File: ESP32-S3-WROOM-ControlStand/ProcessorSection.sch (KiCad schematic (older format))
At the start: 21 parts, among them IC601 USBLC6-2SC6, J601 GCT_USB4105, SW24 RESET, SW601 BOOT, U601 ESP32_S3_WROOM-1

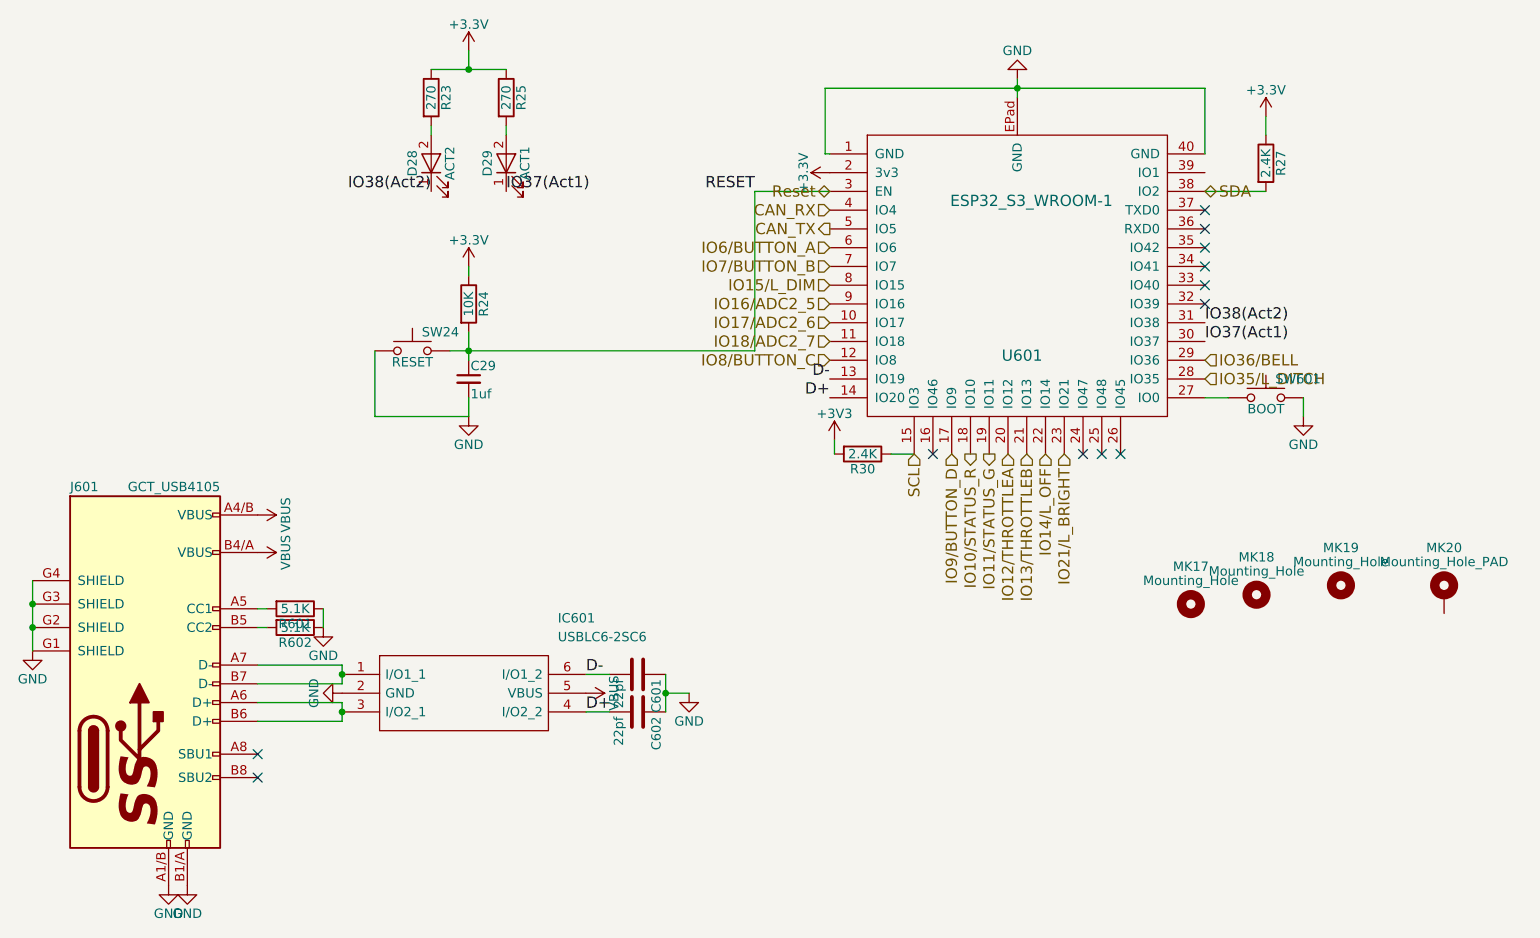
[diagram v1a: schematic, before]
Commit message: Add ESP32-T7S3-ControlStand.
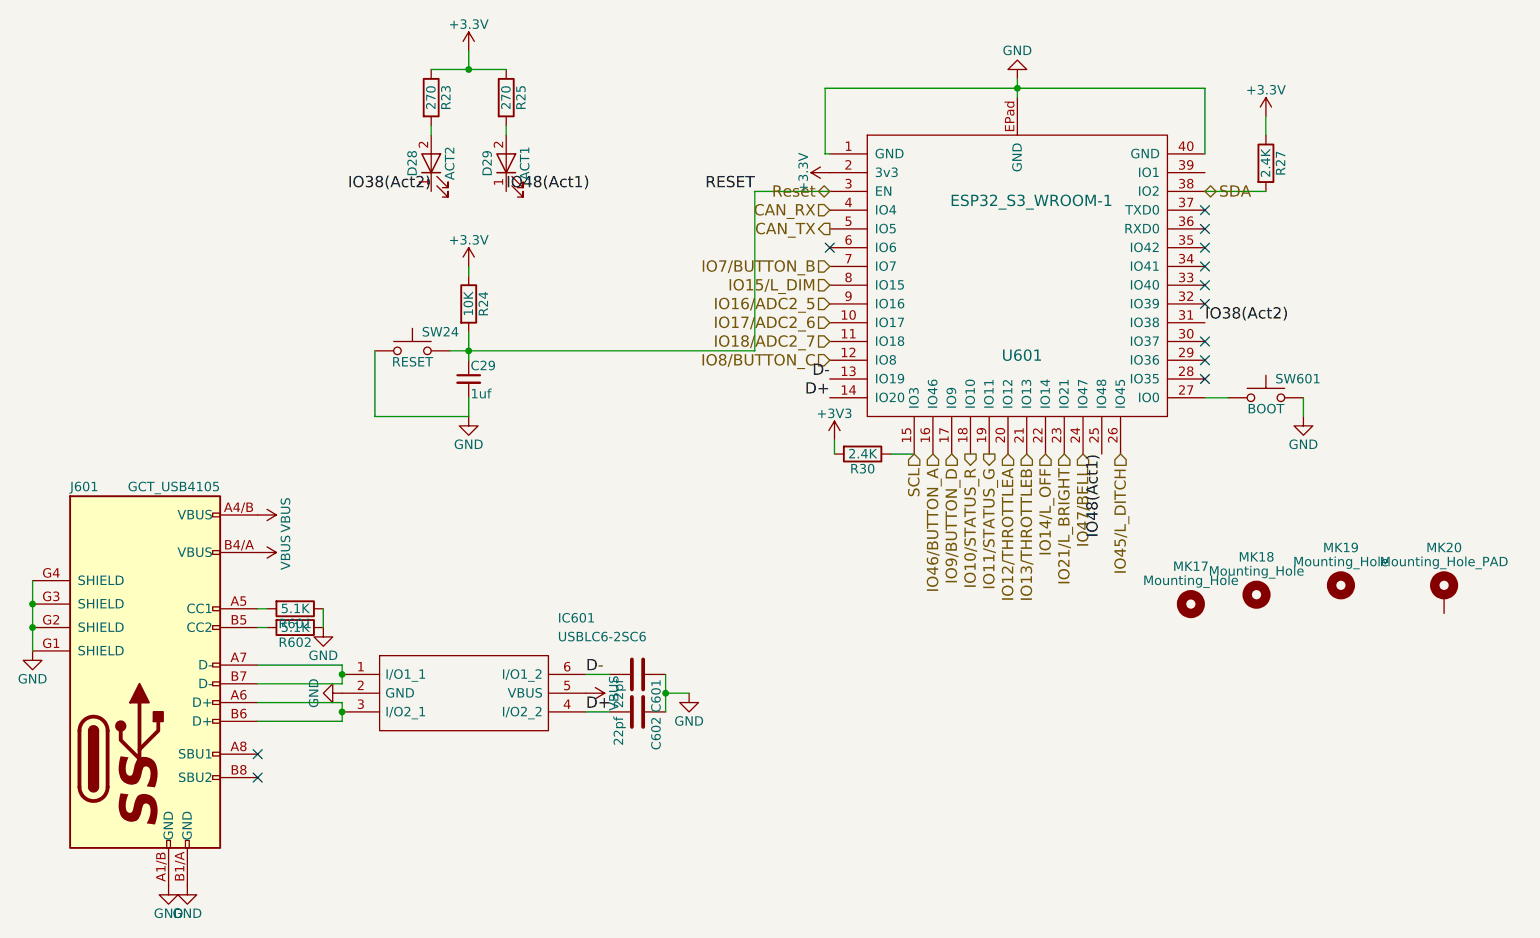
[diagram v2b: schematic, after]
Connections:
- net IO46/BUTTON_A: now reaches U601.16 (IO46)
- net IO47/BELL: now reaches U601.24 (IO47)
- net IO48(Act1): now reaches U601.25 (IO48)
- net IO48(Act1): now also D29.1 (K)
- net IO45/L_DITCH: now reaches U601.26 (IO45)
- net IO35/L_DITCH: no longer names the net of U601.28 (IO35)
- net IO36/BELL: no longer names the net of U601.29 (IO36)
- net IO37(Act1): no longer names the net of U601.30 (IO37)
- net IO37(Act1): no longer D29.1 (K)
- net IO6/BUTTON_A: no longer names the net of U601.6 (IO6)
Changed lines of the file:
@@
 $EndComp
 Text Label 3850 3150 0    60   ~ 0
-IO37(Act1)
+IO48(Act1)
 Text Label 3450 3150 2    60   ~ 0
 IO38(Act2)
@@
 Text HLabel 5575 4050 0    60   Input ~ 0
 IO8/BUTTON_C
-Text HLabel 5575 3450 0    60   Input ~ 0
-IO6/BUTTON_A
+Text HLabel 6125 4550 3    60   Input ~ 0
+IO46/BUTTON_A
 Text HLabel 5575 3550 0    60   Input ~ 0
 IO7/BUTTON_B
@@
 Text HLabel 6825 4550 3    60   Input ~ 0
 IO21/L_BRIGHT
-Text HLabel 7575 4150 2    60   Input ~ 0
-IO35/L_DITCH
+Text HLabel 7125 4550 3    60   Input ~ 0
+IO45/L_DITCH
 $Comp
 L Mounting_Hole MK17
@@
 Wire Wire Line
 	8100 4250 8100 4350
-Text HLabel 7575 4050 2    60   Input ~ 0
-IO36/BELL
-Text Label 7575 3950 0    60   ~ 0
-IO37(Act1)
+Text HLabel 6925 4550 3    60   Input ~ 0
+IO47/BELL
+Text Label 7025 4550 3    60   ~ 0
+IO48(Act1)
 Text Label 7575 3850 0    60   ~ 0
 IO38(Act2)
@@
 NoConn ~ 7575 3350
 NoConn ~ 7575 3250
-NoConn ~ 6125 4550
-NoConn ~ 6925 4550
-NoConn ~ 7025 4550
-NoConn ~ 7125 4550
+NoConn ~ 7575 3950
+NoConn ~ 5575 3450
+NoConn ~ 7575 4150
+NoConn ~ 7575 4050
 $EndSCHEMATC
